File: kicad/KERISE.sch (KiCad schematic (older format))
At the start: 4 parts, among them SW1 SW_Push, U1 ESP32

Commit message: 自動配線成功
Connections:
- no-connect marks 13 -> 12
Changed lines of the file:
@@
 Text GLabel 5600 2200 0    50   Output ~ 0
 SPI-MOSI
-Text Label 5500 1000 2    60   ~ 0
-ANTENA
 $Comp
 L ESP32 U1
@@
 NoConn ~ 5600 2800
 NoConn ~ 5600 4300
-NoConn ~ 5600 1000
 $Comp
 L GND #PWR06
@@
 Wire Wire Line
 	3600 5200 3700 5200
-Wire Wire Line
-	5600 1000 5500 1000
 Wire Wire Line
 	2500 3200 2400 3200
@@
 Text GLabel 5600 3900 0    50   Input ~ 0
 BAT-VOL
+Text Label 5500 1000 2    60   ~ 0
+ANTENA
+Wire Wire Line
+	5600 1000 5500 1000
 $EndSCHEMATC

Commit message: 回路を改良
受光部をフォトトランジスタに変更
測距センサをVL6180Xに変更
動作電圧を3Vに変更
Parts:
- removed U1: ESP32, mouse:ESP32-PICO-D4, symbol ESP32
- added U1: ESP32-PICO-D4, mouse:ESP32-PICO-D4, symbol ESP32-PICO-D4
- SW1: footprint mouse:SW_PUSH -> mouse:SKRPACE010
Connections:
- no-connect marks 12 -> 14
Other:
- moved on the sheet: C1
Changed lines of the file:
@@
 LIBS:ftdi
 LIBS:gennum
-LIBS:graphic
 LIBS:hc11
 LIBS:ir
 LIBS:Lattice
 LIBS:leds
-LIBS:logo
 LIBS:maxim
 LIBS:mechanical
@@
 LIBS:zetex
 LIBS:Zilog
+LIBS:graphic_symbols
+LIBS:infineon
+LIBS:intersil
+LIBS:LEM
+LIBS:logic_programmable
+LIBS:RFSolutions
 LIBS:KERISE-cache
 EELAYER 25 0
@@
 Text GLabel 1300 4700 0    50   Input ~ 0
 FAN
-Text GLabel 5600 3800 0    50   Output ~ 0
+Text GLabel 5600 3500 0    50   Output ~ 0
 FAN
 Text GLabel 5600 3700 0    50   Output ~ 0
@@
 Text GLabel 3700 5500 2    50   Input ~ 0
 SPI-MOSI
+Text GLabel 5600 3800 0    50   Output ~ 0
+SPI-CS-AXIS_1
 Text GLabel 5600 1600 0    50   Output ~ 0
-SPI-CS-AXIS_1
-Text GLabel 5600 1400 0    50   Output ~ 0
 SPI-CS-ENC
 Text GLabel 5600 2100 0    50   Output ~ 0
 SPI-SCLK
-Text GLabel 5600 3500 0    50   Input ~ 0
+Text GLabel 5600 2200 0    50   Input ~ 0
 SPI-MISO
-Text GLabel 5600 2200 0    50   Output ~ 0
+Text GLabel 5600 1400 0    50   Output ~ 0
 SPI-MOSI
-$Comp
-L ESP32 U1
-U 1 1 594A458D
-P 7600 2800
-F 0 "U1" H 7600 4850 60  0000 C CNN
-F 1 "ESP32" H 7600 4700 60  0000 C CNN
-F 2 "mouse:ESP32-PICO-D4" H 7600 4600 60  0001 C CNN
-F 3 "" H 7750 4200 60  0001 C CNN
-	1    7600 2800
-	1    0    0    -1
-$EndComp
 $Comp
 L SW_Push SW1
@@
 F 0 "SW1" H 10050 3400 50  0000 L CNN
 F 1 "SW_Push" H 10000 3240 50  0000 C CNN
-F 2 "mouse:SW_PUSH" H 10000 3500 50  0001 C CNN
+F 2 "mouse:SKRPACE010" H 10000 3500 50  0001 C CNN
 F 3 "" H 10000 3500 50  0001 C CNN
 	1    10000 3300
@@
 Text GLabel 3700 4800 2    50   Input ~ 0
 SPI-MOSI
-Text GLabel 5600 1700 0    50   Output ~ 0
+Text GLabel 5600 3900 0    50   Output ~ 0
 SPI-CS-AXIS_2
 NoConn ~ 9600 2600
@@
 	9700 3100 9600 3100
 Wire Wire Line
-	9700 900  9700 2200
-Wire Wire Line
 	10100 3000 10000 3000
 Wire Wire Line
@@
 Wire Wire Line
 	10100 2900 10100 3000
-Connection ~ 9700 1600
-Connection ~ 9700 1400
-Connection ~ 9700 1200
 Wire Wire Line
 	2500 2000 2400 2000
@@
 	1300 3600 1400 3600
 Wire Wire Line
-	9800 900  9800 2000
-Connection ~ 9800 1000
-Connection ~ 9800 1800
-Wire Wire Line
-	9700 2200 9600 2200
-Wire Wire Line
 	3700 4800 3600 4800
 Wire Wire Line
@@
 Wire Wire Line
 	3600 4500 3700 4500
-Wire Wire Line
-	9700 1600 9600 1600
-Wire Wire Line
-	9800 1000 9600 1000
-Wire Wire Line
-	9800 2000 9600 2000
-Wire Wire Line
-	9600 1800 9800 1800
 Connection ~ 9700 3100
 Wire Wire Line
@@
 Wire Wire Line
 	10300 3400 10300 3300
-Wire Wire Line
-	9700 1200 9600 1200
-Wire Wire Line
-	9600 1400 9900 1400
 $Comp
 L C_Small C1
 U 1 1 58A9401A
-P 10000 1400
-F 0 "C1" H 10010 1470 50  0000 L CNN
-F 1 "10u" H 10010 1320 50  0000 L CNN
-F 2 "Capacitors_SMD:C_0402" H 10000 1400 50  0001 C CNN
-F 3 "" H 10000 1400 50  0000 C CNN
-	1    10000 1400
+P 10000 1000
+F 0 "C1" H 10010 1070 50  0000 L CNN
+F 1 "10u" H 10010 920 50  0000 L CNN
+F 2 "Capacitors_SMD:C_0402" H 10000 1000 50  0001 C CNN
+F 3 "" H 10000 1000 50  0000 C CNN
+	1    10000 1000
 	0    1    1    0
 $EndComp
 Wire Wire Line
-	10200 1400 10100 1400
-Wire Wire Line
-	10200 1400 10200 2300
+	10200 1000 10100 1000
 $Sheet
 S 1400 1200 1000 500
@@
 Text GLabel 5600 3400 0    50   Output ~ 0
 I2C-SCL
-Text GLabel 5600 3900 0    50   Input ~ 0
-BAT-VOL
 Text Label 5500 1000 2    60   ~ 0
 ANTENA
 Wire Wire Line
 	5600 1000 5500 1000
+$Comp
+L ESP32-PICO-D4 U1
+U 1 1 5A515B41
+P 7600 2800
+F 0 "U1" H 7600 4850 60  0000 C CNN
+F 1 "ESP32-PICO-D4" H 7600 4700 60  0000 C CNN
+F 2 "mouse:ESP32-PICO-D4" H 7600 4600 60  0001 C CNN
+F 3 "" H 7750 4200 60  0001 C CNN
+	1    7600 2800
+	1    0    0    -1
+$EndComp
+Wire Wire Line
+	10200 1000 10200 2300
+Wire Wire Line
+	9600 1600 9700 1600
+Wire Wire Line
+	9700 1600 9700 900
+Wire Wire Line
+	9600 1000 9900 1000
+Connection ~ 9700 1000
+Wire Wire Line
+	9600 1200 9700 1200
+Connection ~ 9700 1200
+Wire Wire Line
+	9700 1400 9600 1400
+Connection ~ 9700 1400
+Wire Wire Line
+	9600 2300 9800 2300
+Wire Wire Line
+	9800 2300 9800 900
+Wire Wire Line
+	9600 1900 9800 1900
+Connection ~ 9800 1900
+Wire Wire Line
+	9800 2100 9600 2100
+Connection ~ 9800 2100
+NoConn ~ 5600 1700
+NoConn ~ 5500 1000
 $EndSCHEMATC

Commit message: 電源ラインを配線
あとは自動配線
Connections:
- no-connect marks 14 -> 13
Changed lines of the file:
@@
 Connection ~ 9800 2100
 NoConn ~ 5600 1700
-NoConn ~ 5500 1000
 $EndSCHEMATC

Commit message: 7本残して自動配線終了
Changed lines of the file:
@@
 Text GLabel 5600 3400 0    50   Output ~ 0
 I2C-SCL
-Text Label 5500 1000 2    60   ~ 0
+Text Label 5600 1000 2    60   ~ 0
 ANTENA
-Wire Wire Line
-	5600 1000 5500 1000
 $Comp
 L ESP32-PICO-D4 U1

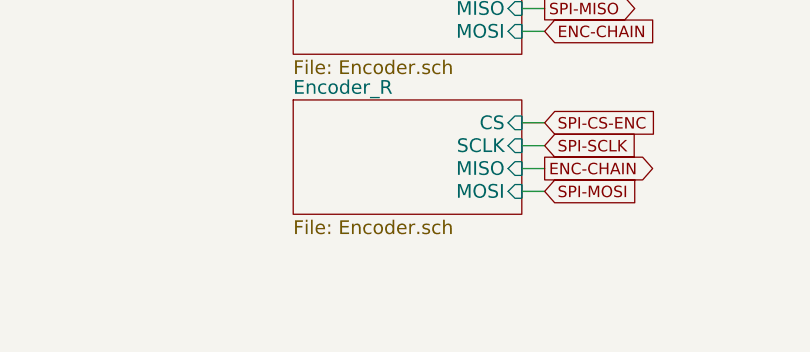
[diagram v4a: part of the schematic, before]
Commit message: 部品を配置
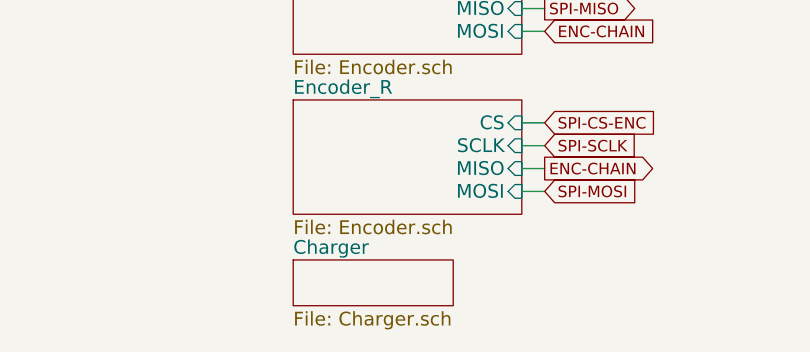
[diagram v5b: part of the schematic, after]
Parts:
- C1: footprint Capacitors_SMD:C_0402 -> Capacitors_SMD:C_0402_NoSilk
- R1: footprint Resistors_SMD:R_0201 -> Resistors_SMD:R_0201_NoSilk
- SW1: footprint mouse:SKRPACE010 -> mouse:EVPBB
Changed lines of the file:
@@
 $Descr A4 11693 8268
 encoding utf-8
-Sheet 1 15
+Sheet 1 16
 Title ""
 Date ""
@@
 F 0 "R1" H 9930 3020 50  0000 L CNN
 F 1 "10k" H 9930 2960 50  0000 L CNN
-F 2 "Resistors_SMD:R_0201" H 9900 3000 50  0001 C CNN
+F 2 "Resistors_SMD:R_0201_NoSilk" H 9900 3000 50  0001 C CNN
 F 3 "" H 9900 3000 50  0000 C CNN
 	1    9900 3000
@@
 F 0 "SW1" H 10050 3400 50  0000 L CNN
 F 1 "SW_Push" H 10000 3240 50  0000 C CNN
-F 2 "mouse:SKRPACE010" H 10000 3500 50  0001 C CNN
+F 2 "mouse:EVPBB" H 10000 3500 50  0001 C CNN
 F 3 "" H 10000 3500 50  0001 C CNN
 	1    10000 3300
@@
 	1    0    0    -1
 $EndComp
-Wire Wire Line
-	9700 3100 9600 3100
-Wire Wire Line
-	10100 3000 10000 3000
-Wire Wire Line
-	9800 3000 9700 3000
-Wire Wire Line
-	10100 2900 10100 3000
-Wire Wire Line
-	2500 2000 2400 2000
-Wire Wire Line
-	1300 2000 1400 2000
-Wire Wire Line
-	9700 4900 9600 4900
-Wire Wire Line
-	9700 5000 9700 4900
-Wire Wire Line
-	1300 4700 1400 4700
-Wire Wire Line
-	1300 4000 1400 4000
-Wire Wire Line
-	1400 4100 1300 4100
-Wire Wire Line
-	2500 2400 2400 2400
-Wire Wire Line
-	2500 2800 2400 2800
-Wire Wire Line
-	2500 900  2400 900
-Wire Wire Line
-	1300 1300 1400 1300
-Wire Wire Line
-	1400 1400 1300 1400
-Wire Wire Line
-	2400 1300 2500 1300
-Wire Wire Line
-	1300 2400 1400 2400
-Wire Wire Line
-	1300 2800 1400 2800
-Wire Wire Line
-	1400 1600 1300 1600
-Wire Wire Line
-	1300 4200 1400 4200
-Wire Wire Line
-	1400 4300 1300 4300
-Wire Wire Line
-	3700 4100 3600 4100
-Wire Wire Line
-	3600 4000 3700 4000
-Wire Wire Line
-	3700 6700 3600 6700
-Wire Wire Line
-	3600 6800 3700 6800
-Wire Wire Line
-	3700 6900 3600 6900
-Wire Wire Line
-	3600 6600 3700 6600
-Wire Wire Line
-	3700 6200 3600 6200
-Wire Wire Line
-	3600 6100 3700 6100
-Wire Wire Line
-	3700 6000 3600 6000
-Wire Wire Line
-	3600 5900 3700 5900
-Wire Wire Line
-	3700 5500 3600 5500
-Wire Wire Line
-	3600 5400 3700 5400
-Wire Wire Line
-	3700 5300 3600 5300
-Wire Wire Line
-	3600 5200 3700 5200
-Wire Wire Line
-	2500 3200 2400 3200
-Wire Wire Line
-	2500 3600 2400 3600
-Wire Wire Line
-	1300 3200 1400 3200
-Wire Wire Line
-	1300 3600 1400 3600
-Wire Wire Line
-	3700 4800 3600 4800
-Wire Wire Line
-	3600 4700 3700 4700
-Wire Wire Line
-	3700 4600 3600 4600
-Wire Wire Line
-	3600 4500 3700 4500
-Connection ~ 9700 3100
-Wire Wire Line
-	9700 3000 9700 3300
-Wire Wire Line
-	9700 3300 9800 3300
-Wire Wire Line
-	10300 3300 10200 3300
-Wire Wire Line
-	10300 3400 10300 3300
 $Comp
 L C_Small C1
@@
 F 0 "C1" H 10010 1070 50  0000 L CNN
 F 1 "10u" H 10010 920 50  0000 L CNN
-F 2 "Capacitors_SMD:C_0402" H 10000 1000 50  0001 C CNN
+F 2 "Capacitors_SMD:C_0402_NoSilk" H 10000 1000 50  0001 C CNN
 F 3 "" H 10000 1000 50  0000 C CNN
 	1    10000 1000
 	0    1    1    0
 $EndComp
-Wire Wire Line
-	10200 1000 10100 1000
 $Sheet
 S 1400 1200 1000 500
@@
 	1    0    0    -1
 $EndComp
+NoConn ~ 5600 1700
+$Sheet
+S 2600 7200 700  200
+U 5AB8C3CF
+F0 "Charger" 60
+F1 "Charger.sch" 60
+$EndSheet
+Wire Wire Line
+	9700 3100 9600 3100
+Wire Wire Line
+	10100 3000 10000 3000
+Wire Wire Line
+	9800 3000 9700 3000
+Wire Wire Line
+	10100 2900 10100 3000
+Wire Wire Line
+	2500 2000 2400 2000
+Wire Wire Line
+	1300 2000 1400 2000
+Wire Wire Line
+	9700 4900 9600 4900
+Wire Wire Line
+	9700 5000 9700 4900
+Wire Wire Line
+	1300 4700 1400 4700
+Wire Wire Line
+	1300 4000 1400 4000
+Wire Wire Line
+	1400 4100 1300 4100
+Wire Wire Line
+	2500 2400 2400 2400
+Wire Wire Line
+	2500 2800 2400 2800
+Wire Wire Line
+	2500 900  2400 900
+Wire Wire Line
+	1300 1300 1400 1300
+Wire Wire Line
+	1400 1400 1300 1400
+Wire Wire Line
+	2400 1300 2500 1300
+Wire Wire Line
+	1300 2400 1400 2400
+Wire Wire Line
+	1300 2800 1400 2800
+Wire Wire Line
+	1400 1600 1300 1600
+Wire Wire Line
+	1300 4200 1400 4200
+Wire Wire Line
+	1400 4300 1300 4300
+Wire Wire Line
+	3700 4100 3600 4100
+Wire Wire Line
+	3600 4000 3700 4000
+Wire Wire Line
+	3700 6700 3600 6700
+Wire Wire Line
+	3600 6800 3700 6800
+Wire Wire Line
+	3700 6900 3600 6900
+Wire Wire Line
+	3600 6600 3700 6600
+Wire Wire Line
+	3700 6200 3600 6200
+Wire Wire Line
+	3600 6100 3700 6100
+Wire Wire Line
+	3700 6000 3600 6000
+Wire Wire Line
+	3600 5900 3700 5900
+Wire Wire Line
+	3700 5500 3600 5500
+Wire Wire Line
+	3600 5400 3700 5400
+Wire Wire Line
+	3700 5300 3600 5300
+Wire Wire Line
+	3600 5200 3700 5200
+Wire Wire Line
+	2500 3200 2400 3200
+Wire Wire Line
+	2500 3600 2400 3600
+Wire Wire Line
+	1300 3200 1400 3200
+Wire Wire Line
+	1300 3600 1400 3600
+Wire Wire Line
+	3700 4800 3600 4800
+Wire Wire Line
+	3600 4700 3700 4700
+Wire Wire Line
+	3700 4600 3600 4600
+Wire Wire Line
+	3600 4500 3700 4500
+Connection ~ 9700 3100
+Wire Wire Line
+	9700 3000 9700 3300
+Wire Wire Line
+	9700 3300 9800 3300
+Wire Wire Line
+	10300 3300 10200 3300
+Wire Wire Line
+	10300 3400 10300 3300
+Wire Wire Line
+	10200 1000 10100 1000
 Wire Wire Line
 	10200 1000 10200 2300
@@
 	9800 2100 9600 2100
 Connection ~ 9800 2100
-NoConn ~ 5600 1700
 $EndSCHEMATC

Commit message: 回路を編集 ToFを除去
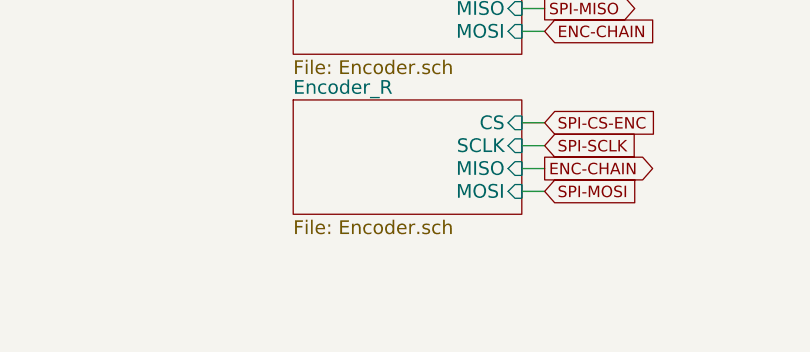
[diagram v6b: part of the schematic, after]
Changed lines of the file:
@@
 $Descr A4 11693 8268
 encoding utf-8
-Sheet 1 16
+Sheet 1 15
 Title ""
 Date ""
@@
 $EndComp
 NoConn ~ 5600 1700
-$Sheet
-S 2600 7200 700  200
-U 5AB8C3CF
-F0 "Charger" 60
-F1 "Charger.sch" 60
-$EndSheet
 Wire Wire Line
 	9700 3100 9600 3100

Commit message: 部品を配置 kicad5
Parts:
- removed SW1: SW_Push, mouse:EVPBB, symbol SW_Push
- added SW1: RESET, mouse:EVPBB, symbol Switch:SW_Push
- C1: symbol C_Small -> Device:C_Small
- R1: symbol R_Small -> Device:R_Small
- U1: symbol ESP32-PICO-D4 -> KERISE:ESP32-PICO-D4
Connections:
- net GND: now also SW1.2
- net at R1.1, U1.9 (CHIP_PU): now also SW1.1
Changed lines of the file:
@@
-EESchema Schematic File Version 2
-LIBS:power
-LIBS:device
-LIBS:transistors
-LIBS:conn
-LIBS:linear
-LIBS:regul
-LIBS:74xx
-LIBS:cmos4000
-LIBS:adc-dac
-LIBS:memory
-LIBS:xilinx
-LIBS:microcontrollers
-LIBS:dsp
-LIBS:microchip
-LIBS:analog_switches
-LIBS:motorola
-LIBS:texas
-LIBS:intel
-LIBS:audio
-LIBS:interface
-LIBS:digital-audio
-LIBS:philips
-LIBS:display
-LIBS:cypress
-LIBS:siliconi
-LIBS:opto
-LIBS:atmel
-LIBS:contrib
-LIBS:valves
-LIBS:KERISE
-LIBS:74xgxx
-LIBS:ac-dc
-LIBS:actel
-LIBS:allegro
-LIBS:Altera
-LIBS:analog_devices
-LIBS:battery_management
-LIBS:bbd
-LIBS:bosch
-LIBS:brooktre
-LIBS:cmos_ieee
-LIBS:dc-dc
-LIBS:diode
-LIBS:elec-unifil
-LIBS:ESD_Protection
-LIBS:ftdi
-LIBS:gennum
-LIBS:hc11
-LIBS:ir
-LIBS:Lattice
-LIBS:leds
-LIBS:maxim
-LIBS:mechanical
-LIBS:microchip_dspic33dsc
-LIBS:microchip_pic10mcu
-LIBS:microchip_pic12mcu
-LIBS:microchip_pic16mcu
-LIBS:microchip_pic18mcu
-LIBS:microchip_pic24mcu
-LIBS:microchip_pic32mcu
-LIBS:modules
-LIBS:motor_drivers
-LIBS:motors
-LIBS:msp430
-LIBS:nordicsemi
-LIBS:nxp
-LIBS:nxp_armmcu
-LIBS:onsemi
-LIBS:Oscillators
-LIBS:Power_Management
-LIBS:powerint
-LIBS:pspice
-LIBS:references
-LIBS:relays
-LIBS:rfcom
-LIBS:sensors
-LIBS:silabs
-LIBS:stm8
-LIBS:stm32
-LIBS:supertex
-LIBS:switches
-LIBS:transf
-LIBS:triac_thyristor
-LIBS:ttl_ieee
-LIBS:video
-LIBS:wiznet
-LIBS:Worldsemi
-LIBS:Xicor
-LIBS:zetex
-LIBS:Zilog
-LIBS:graphic_symbols
-LIBS:infineon
-LIBS:intersil
-LIBS:LEM
-LIBS:logic_programmable
-LIBS:RFSolutions
+EESchema Schematic File Version 4
 LIBS:KERISE-cache
-EELAYER 25 0
+EELAYER 26 0
 EELAYER END
 $Descr A4 11693 8268
 encoding utf-8
-Sheet 1 15
+Sheet 1 14
 Title ""
 Date ""
@@
 BUTTON
 $Comp
-L GND #PWR01
+L power:GND #PWR06
 U 1 1 58964ED8
 P 10300 3400
-F 0 "#PWR01" H 10300 3150 50  0001 C CNN
+F 0 "#PWR06" H 10300 3150 50  0001 C CNN
 F 1 "GND" H 10300 3250 50  0000 C CNN
 F 2 "" H 10300 3400 50  0000 C CNN
@@
 UART-RX
 $Comp
-L +3.3V #PWR02
+L power:+3.3V #PWR04
 U 1 1 58A4281C
 P 10100 2900
-F 0 "#PWR02" H 10100 2750 50  0001 C CNN
+F 0 "#PWR04" H 10100 2750 50  0001 C CNN
 F 1 "+3.3V" H 10100 3040 50  0000 C CNN
 F 2 "" H 10100 2900 50  0000 C CNN
@@
 $EndComp
 $Comp
-L R_Small R1
+L Device:R_Small R1
 U 1 1 58A7844B
 P 9900 3000
@@
 	0    -1   -1   0
 $EndComp
-$Comp
-L +3.3V #PWR03
-U 1 1 58A831D9
-P 9700 900
-F 0 "#PWR03" H 9700 750 50  0001 C CNN
-F 1 "+3.3V" H 9650 1050 50  0000 C CNN
-F 2 "" H 9700 900 50  0000 C CNN
-F 3 "" H 9700 900 50  0000 C CNN
-	1    9700 900
-	1    0    0    -1
-$EndComp
 $Sheet
 S 2600 6500 1000 500
@@
 F4 "MISO" I R 3600 6800 60
 F5 "MOSI" I R 3600 6900 60
-$EndSheet
-Text GLabel 3700 4000 2    50   Input ~ 0
-I2C-SDA
-Text GLabel 3700 4100 2    50   Input ~ 0
-I2C-SCL
-$Sheet
-S 2600 3900 1000 300
-U 592B9AF5
-F0 "ToF" 60
-F1 "ToF.sch" 60
-F2 "SDA" I R 3600 4000 60
-F3 "SCL" I R 3600 4100 60
 $EndSheet
 $Sheet
@@
 Text GLabel 5600 1400 0    50   Output ~ 0
 SPI-MOSI
-$Comp
-L SW_Push SW1
-U 1 1 594AEB3C
-P 10000 3300
-F 0 "SW1" H 10050 3400 50  0000 L CNN
-F 1 "SW_Push" H 10000 3240 50  0000 C CNN
-F 2 "mouse:EVPBB" H 10000 3500 50  0001 C CNN
-F 3 "" H 10000 3500 50  0001 C CNN
-	1    10000 3300
-	1    0    0    -1
-$EndComp
 Text GLabel 2500 3200 2    50   Output ~ 0
 PR-RCV-FL
@@
 PR-RCV-FR
 $Comp
-L VDDA #PWR04
+L power:VDDA #PWR03
 U 1 1 59C3BA09
 P 9800 900
-F 0 "#PWR04" H 9800 750 50  0001 C CNN
+F 0 "#PWR03" H 9800 750 50  0001 C CNN
 F 1 "VDDA" H 9900 1050 50  0000 C CNN
 F 2 "" H 9800 900 50  0001 C CNN
@@
 NoConn ~ 9600 4100
 NoConn ~ 9600 3700
-$Comp
-L GND #PWR05
-U 1 1 5A1B6298
-P 9700 5000
-F 0 "#PWR05" H 9700 4750 50  0001 C CNN
-F 1 "GND" H 9700 4850 50  0000 C CNN
-F 2 "" H 9700 5000 50  0000 C CNN
-F 3 "" H 9700 5000 50  0000 C CNN
-	1    9700 5000
-	1    0    0    -1
-$EndComp
 NoConn ~ 5600 2900
 NoConn ~ 5600 2800
 NoConn ~ 5600 4300
 $Comp
-L GND #PWR06
+L power:GND #PWR05
 U 1 1 58A70C45
 P 10200 2300
-F 0 "#PWR06" H 10200 2050 50  0001 C CNN
+F 0 "#PWR05" H 10200 2050 50  0001 C CNN
 F 1 "GND" H 10200 2150 50  0000 C CNN
 F 2 "" H 10200 2300 50  0000 C CNN
@@
 $EndComp
 $Comp
-L C_Small C1
+L Device:C_Small C1
 U 1 1 58A9401A
 P 10000 1000
@@
 ANTENA
 $Comp
-L ESP32-PICO-D4 U1
+L KERISE:ESP32-PICO-D4 U1
 U 1 1 5A515B41
 P 7600 2800
@@
 	1400 4300 1300 4300
 Wire Wire Line
-	3700 4100 3600 4100
-Wire Wire Line
-	3600 4000 3700 4000
-Wire Wire Line
 	3700 6700 3600 6700
 Wire Wire Line
@@
 Connection ~ 9700 3100
 Wire Wire Line
-	9700 3000 9700 3300
+	9700 3000 9700 3100
 Wire Wire Line
 	9700 3300 9800 3300
@@
 	9600 1600 9700 1600
 Wire Wire Line
-	9700 1600 9700 900
-Wire Wire Line
-	9600 1000 9900 1000
+	9700 1600 9700 1400
+Wire Wire Line
+	9600 1000 9700 1000
 Connection ~ 9700 1000
 Wire Wire Line
@@
 	9600 2300 9800 2300
 Wire Wire Line
-	9800 2300 9800 900
+	9800 2300 9800 2100
 Wire Wire Line
 	9600 1900 9800 1900
@@
 	9800 2100 9600 2100
 Connection ~ 9800 2100
+Wire Wire Line
+	9700 3100 9700 3300
+Wire Wire Line
+	9700 1000 9700 900
+Wire Wire Line
+	9700 1000 9900 1000
+Wire Wire Line
+	9700 1200 9700 1000
+Wire Wire Line
+	9700 1400 9700 1200
+Wire Wire Line
+	9800 1900 9800 900
+Wire Wire Line
+	9800 2100 9800 1900
+$Comp
+L Switch:SW_Push SW1
+U 1 1 5B6F20EF
+P 10000 3300
+F 0 "SW1" H 10000 3450 50  0000 C CNN
+F 1 "RESET" H 10000 3200 50  0000 C CNN
+F 2 "mouse:EVPBB" H 10000 3500 50  0001 C CNN
+F 3 "" H 10000 3500 50  0001 C CNN
+	1    10000 3300
+	1    0    0    -1
+$EndComp
+$Comp
+L power:GND #PWR02
+U 1 1 5B709AF6
+P 9700 5000
+F 0 "#PWR02" H 9700 4750 50  0001 C CNN
+F 1 "GND" H 9700 4850 50  0000 C CNN
+F 2 "" H 9700 5000 50  0000 C CNN
+F 3 "" H 9700 5000 50  0000 C CNN
+	1    9700 5000
+	1    0    0    -1
+$EndComp
+$Comp
+L power:+3.3V #PWR01
+U 1 1 5B709B26
+P 9700 900
+F 0 "#PWR01" H 9700 750 50  0001 C CNN
+F 1 "+3.3V" H 9600 1050 50  0000 C CNN
+F 2 "" H 9700 900 50  0000 C CNN
+F 3 "" H 9700 900 50  0000 C CNN
+	1    9700 900
+	1    0    0    -1
+$EndComp
 $EndSCHEMATC
